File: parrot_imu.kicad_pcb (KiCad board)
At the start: 2 copper layers, 50.8 x 61 mm, 25 parts, among them J1 Conn_01x02_Male, J2 SI-60062-F, J3 TB005-762-02BE, U1 TR05S3V3, U2 VR10S05, U3 Spark_fun_ICM-20948, U4 Teensy4.1, U5 TJA1441AT/0Z, U6 ESDCAN24-2BLY

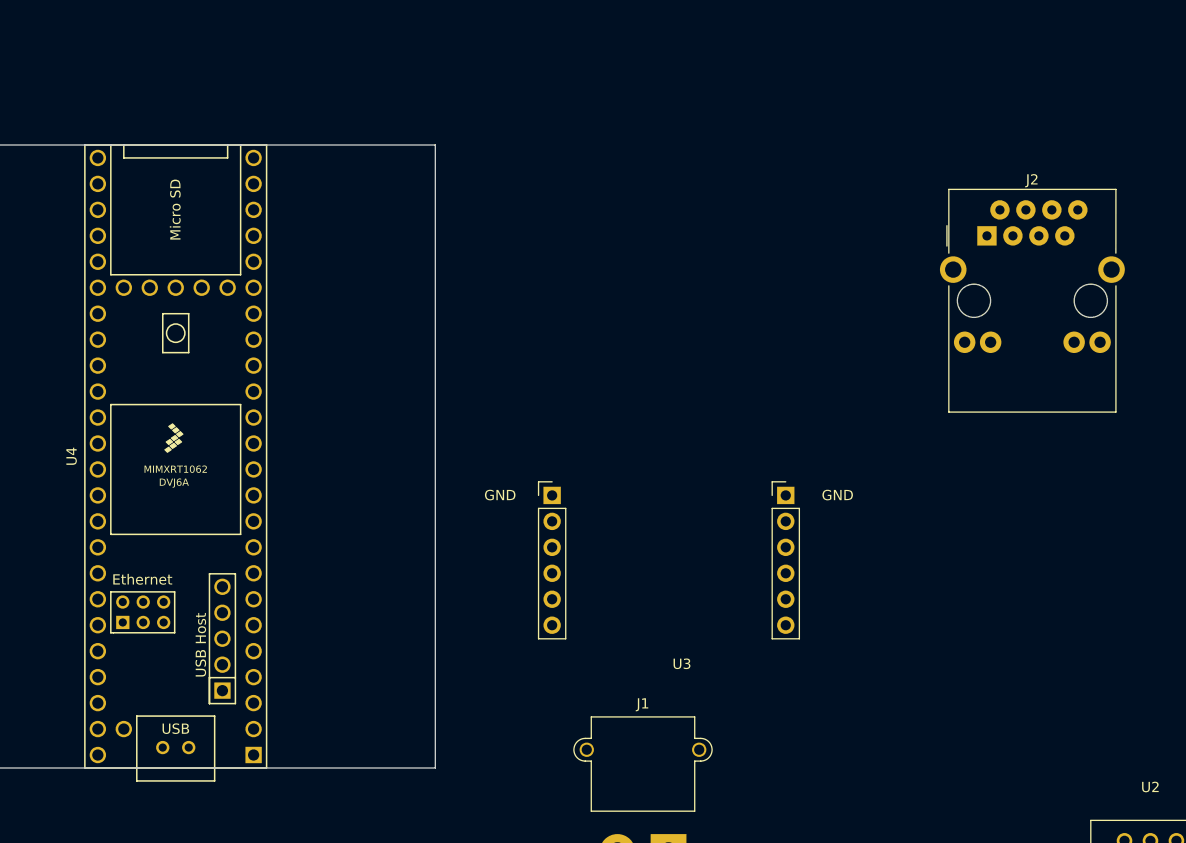
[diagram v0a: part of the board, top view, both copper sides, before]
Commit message: sort out errors with footprints and add mounting holes
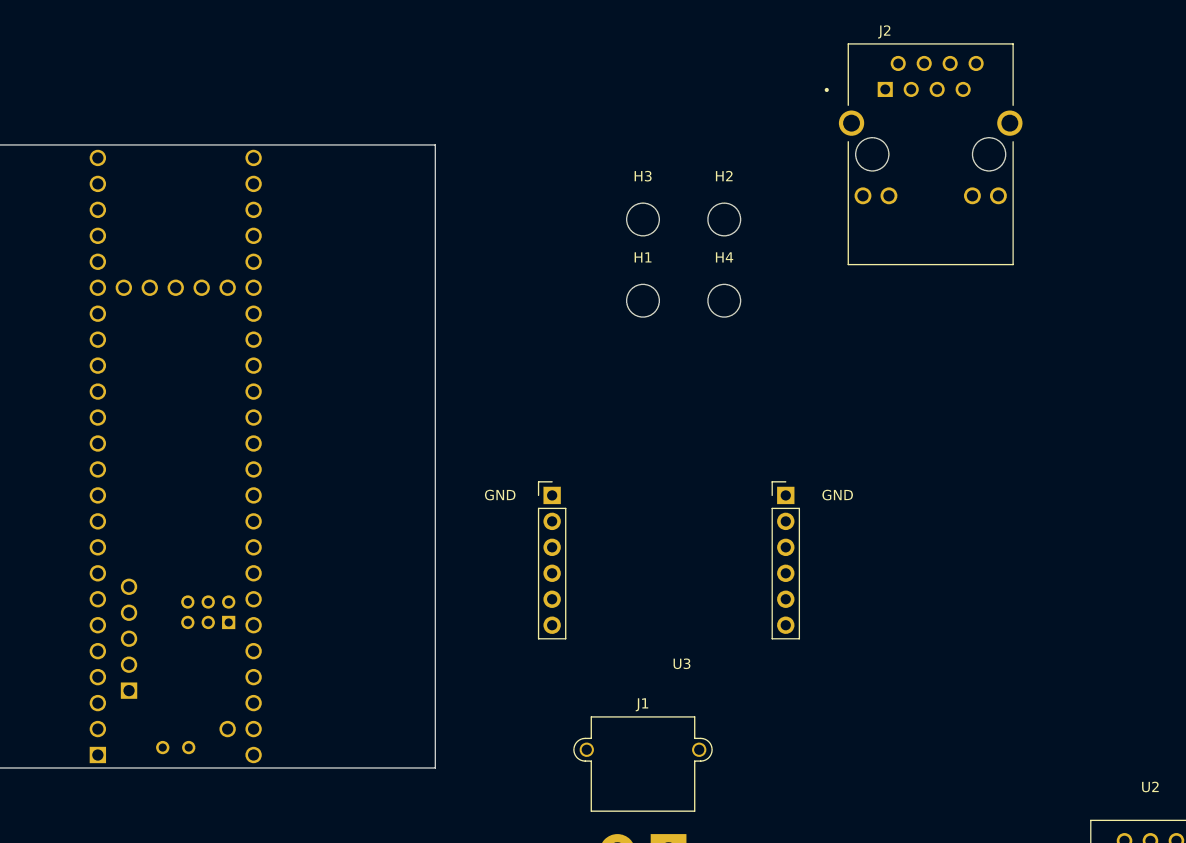
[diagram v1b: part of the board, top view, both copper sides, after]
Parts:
- added H1: MountingHole, MountingHole:MountingHole_3.2mm_M3, F.Cu at (116.8, 63.5)
- added H2: MountingHole, MountingHole:MountingHole_3.2mm_M3, F.Cu at (124.8, 55.5)
- added H3: MountingHole, MountingHole:MountingHole_3.2mm_M3, F.Cu at (116.8, 55.5)
- added H4: MountingHole, MountingHole:MountingHole_3.2mm_M3, F.Cu at (124.8, 63.5)
- J2: footprint Connector_RJ:RJ45_Bel_SI-60062-F -> magjack:BEL_SI-60062-F
- U4: moved to B.Cu
- moved J2 9.69 mm to (145.0, 49.2)

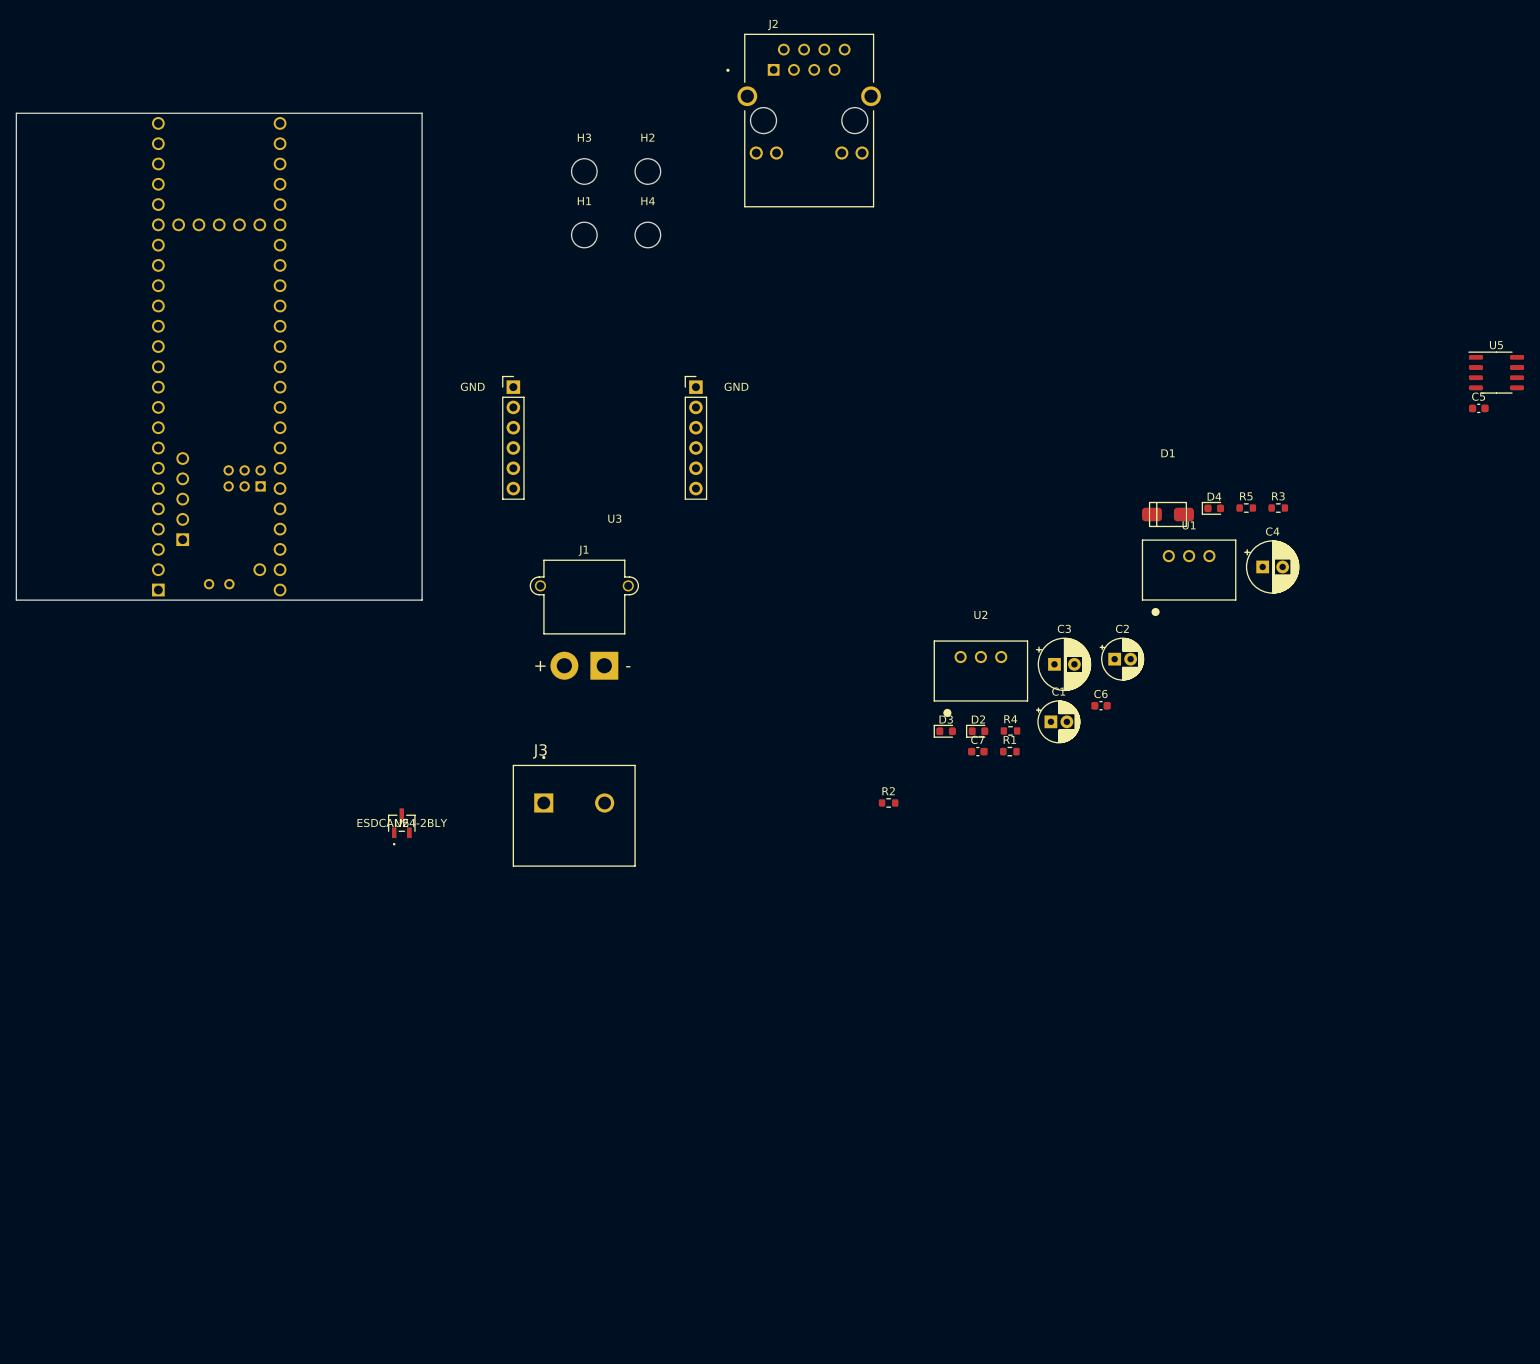
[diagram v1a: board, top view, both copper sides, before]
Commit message: start of laying out components
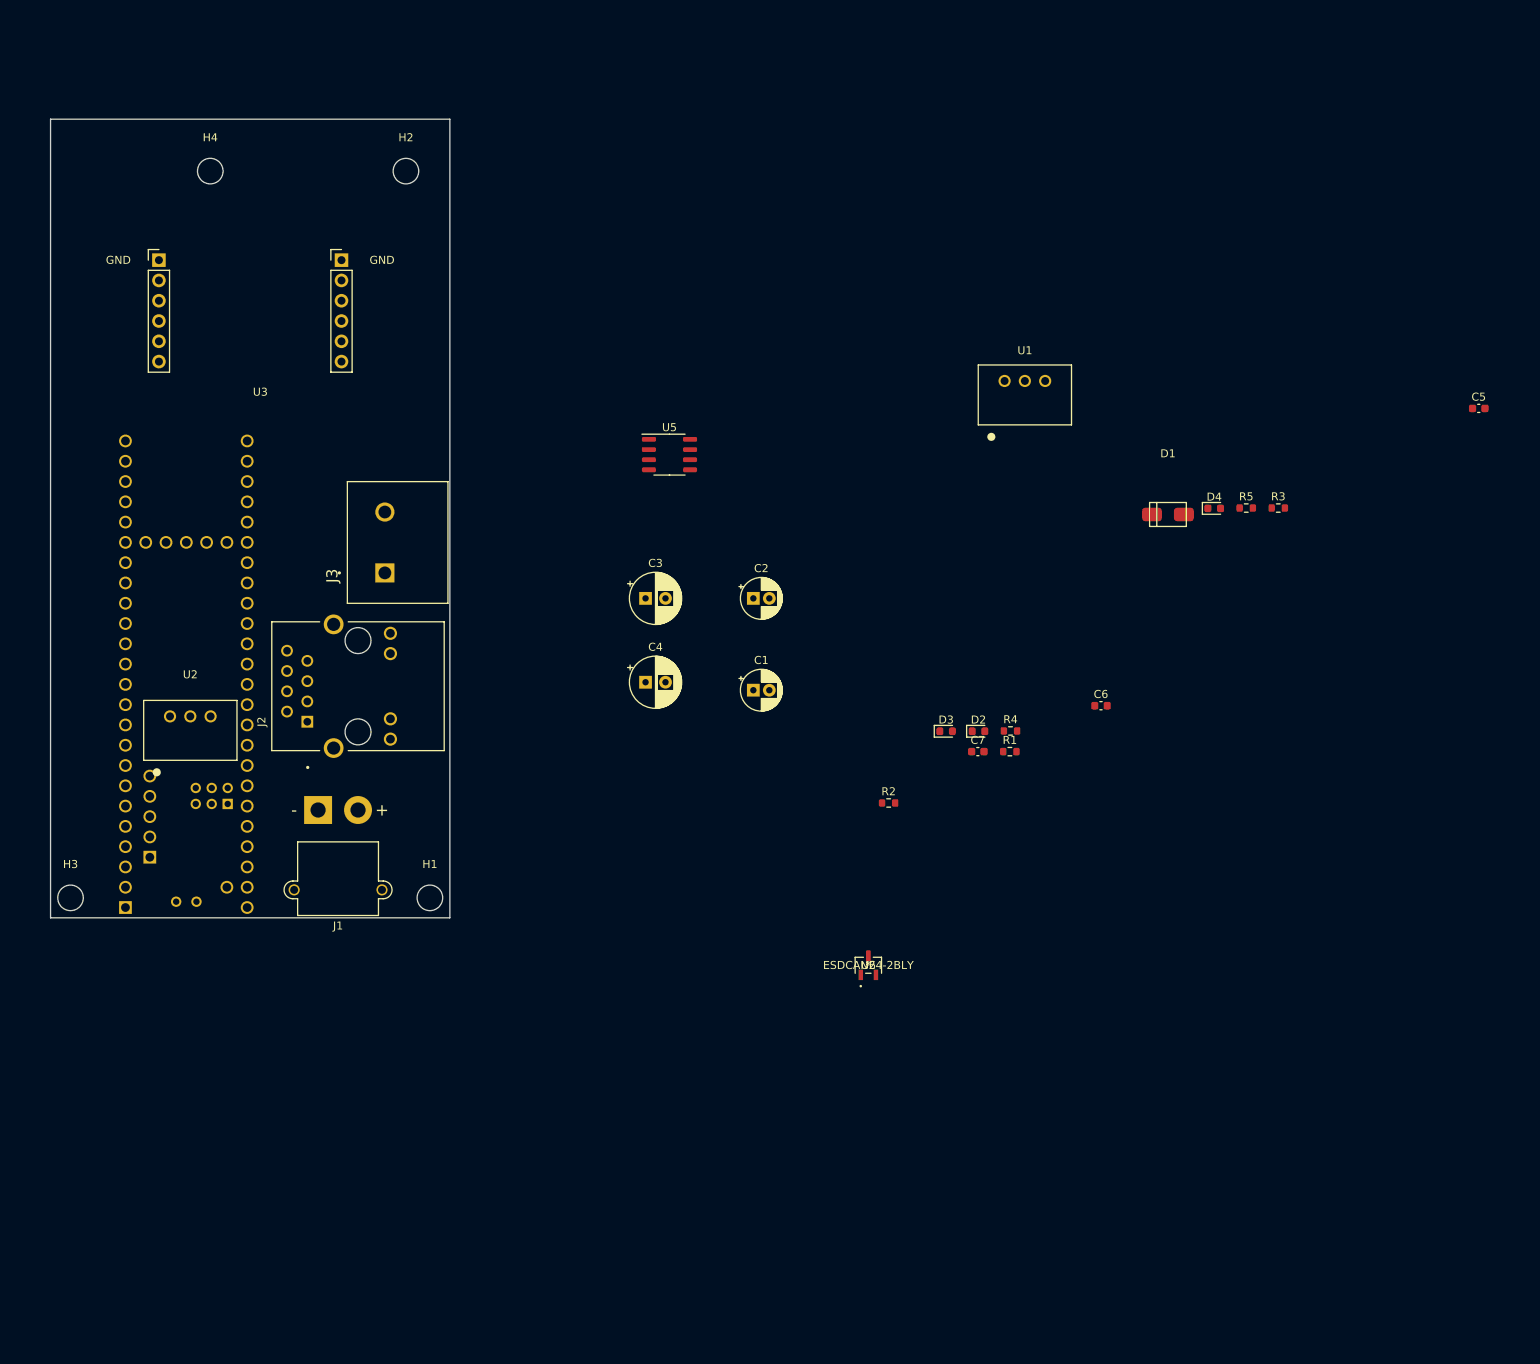
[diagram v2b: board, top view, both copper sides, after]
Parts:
- moved H3 111.4 mm to (52.5, 146.5)
- moved U5 104.1 mm to (127.5, 91.0)
- moved U2 99.3 mm to (67.5, 123.8)
- moved J2 90.6 mm to (88.5, 120.0), turned to 90 degrees
- moved H1 85.2 mm to (97.5, 146.5)
- moved C4 78.6 mm to (124.5, 119.5)
- moved U6 61.1 mm to (152.4, 154.9)
- moved H4 55.4 mm to (70.0, 55.5)
- moved C3 51.9 mm to (124.5, 109.0)
- moved U3 47.1 mm to (86.4, 71.7)
- moved C2 45.9 mm to (138.0, 109.0)
- moved J1 40.1 mm to (83.5, 135.5), turned to 180 degrees
- moved U4 40.0 mm to (67.0, 118.5)
- moved C1 37.5 mm to (138.0, 120.5)
- moved J3 35.0 mm to (91.9, 105.8), turned to 90 degrees
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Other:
- board size 50.8 x 61 mm -> 50 x 100 mm

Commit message: most of pcb and some steps
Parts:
- C6, C7, R4, R5, U5, U6: moved to B.Cu
- J1: footprint Connector_AMASS:AMASS_XT30PW-M_1x02_P2.50mm_Horizontal -> Connector_AMASS:AMASS_XT30PW-F_1x02_P2.50mm_Horizontal
- U4: moved to F.Cu
- moved C5 156.8 mm to (72.0, 82.8), turned to 90 degrees
- moved R3 144.4 mm to (61.5, 122.5), turned to -90 degrees
- moved D4 135.1 mm to (63.2, 124.2), turned to 90 degrees
- moved R5 113.2 mm to (87.3, 84.5), turned to 90 degrees
- moved D1 108.6 mm to (86.0, 130.0)
- moved U1 104.6 mm to (76.5, 124.5), turned to 90 degrees
- moved C7 100.4 mm to (76.5, 82.9), turned to 180 degrees
- moved U6 96.9 mm to (83.7, 86.6), turned to 90 degrees
- moved C6 96.4 mm to (86.5, 106.5), turned to 90 degrees
- moved R4 90.8 mm to (87.3, 88.5), turned to 90 degrees
- moved R1 79.1 mm to (91.0, 126.5), turned to -90 degrees
- moved C2 74.4 mm to (68.5, 135.5), turned to 90 degrees
- moved D3 74.0 mm to (88.5, 118.7), turned to -90 degrees
- moved C3 73.7 mm to (54.0, 130.3), turned to -90 degrees
- moved D2 73.2 mm to (93.0, 126.4), turned to -90 degrees
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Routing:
- net /MOSI: track 0.00 -> 60.4 mm
- net /CS: track 0.00 -> 59.7 mm
- net /SCK: track 0.00 -> 58.9 mm
- net /MISO: track 0.00 -> 57.7 mm
- net /Eth_led: track 0.00 -> 54.3 mm
- net Net-(C1-Pad1): track 0.00 -> 51.2 mm
- net /Eth_tx-: track 0.00 -> 44.6 mm
- net /Eth_tx+: track 0.00 -> 44.0 mm
- net /Eth_rx+: track 0.00 -> 40.7 mm
- net /Eth_rx-: track 0.00 -> 34.7 mm
- net /Can_rx: track 0.00 -> 21.4 mm
- net /Can_tx: track 0.00 -> 21.2 mm
- net +3.3V: track 0.00 -> 17.5 mm, vias 0 -> 1
- net +5V: track 0.00 -> 14.7 mm, vias 0 -> 1
- net GND: track 0.00 -> 8.23 mm, vias 0 -> 4
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- added copper zone on F.Cu, net +3.3V
- added copper zone on F.Cu, net +5V
- added copper zone on B.Cu, net GND

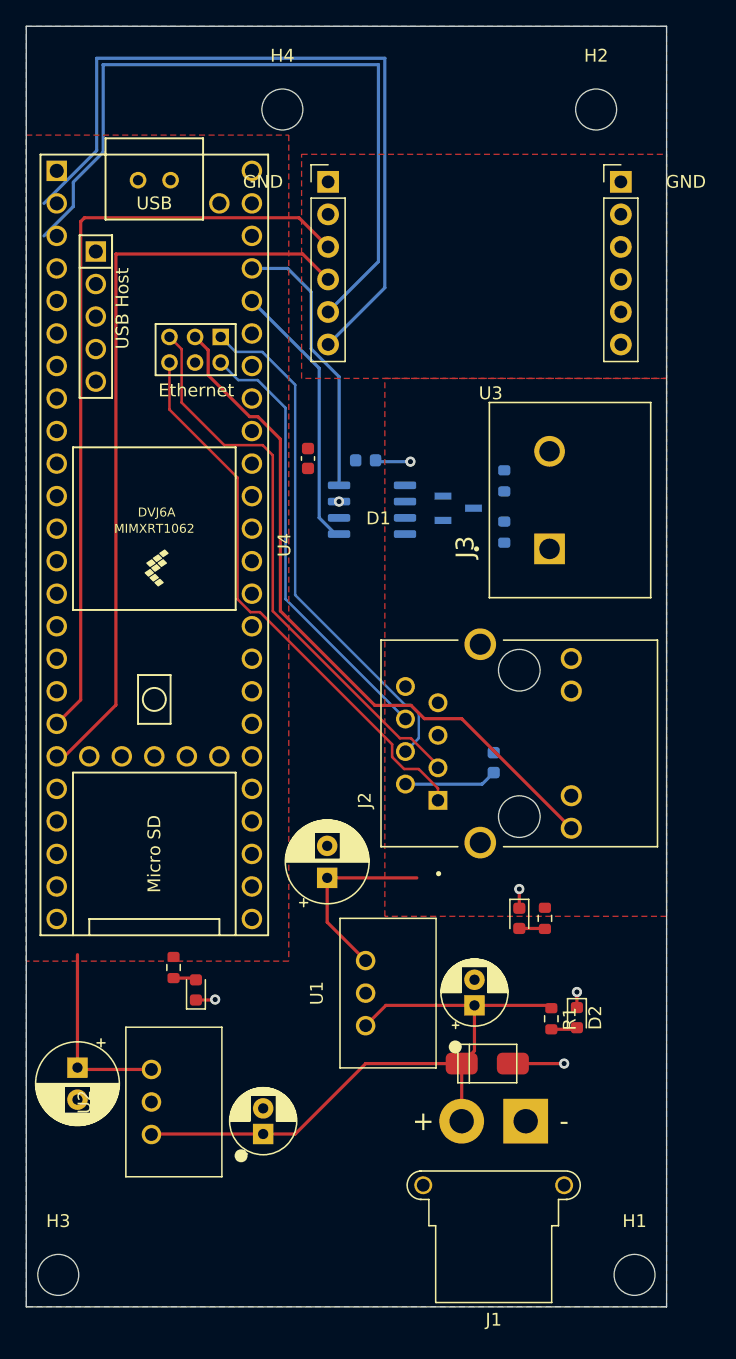
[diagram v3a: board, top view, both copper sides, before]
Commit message: completed draft pcb and added model for imu
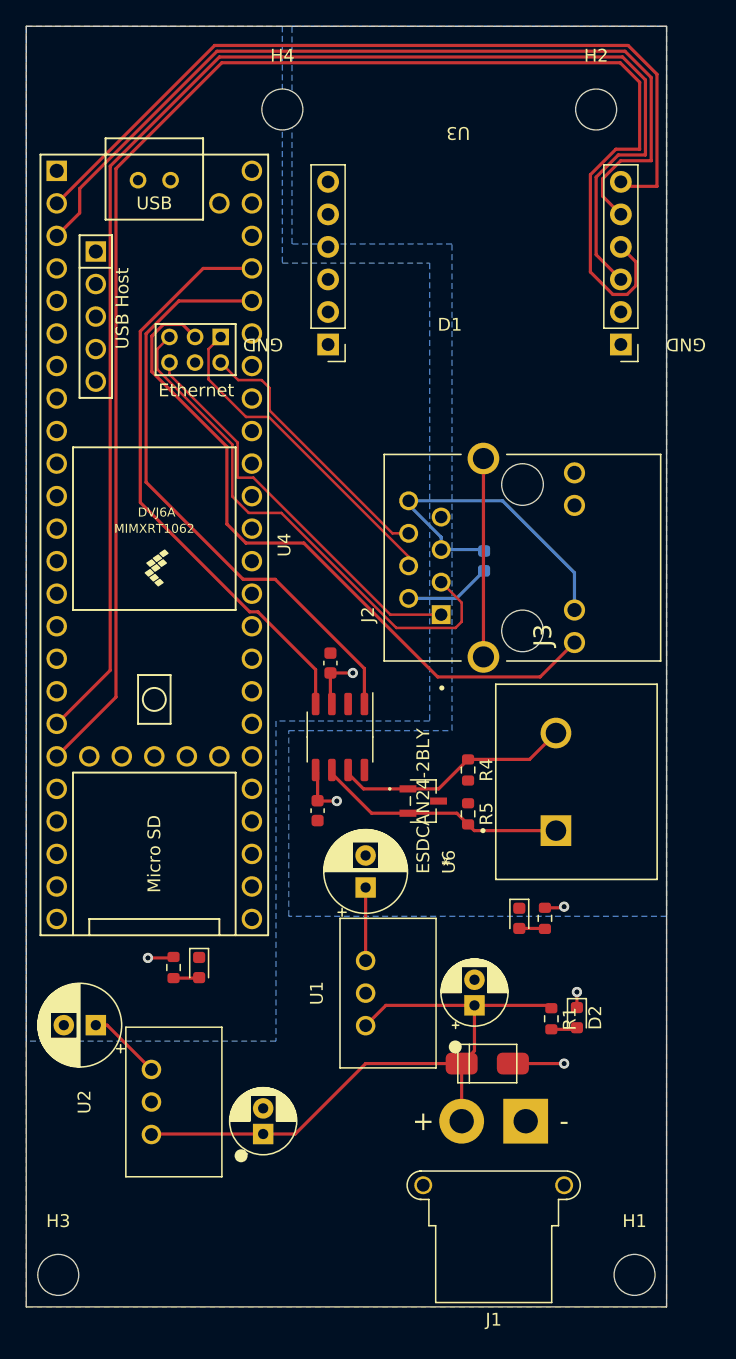
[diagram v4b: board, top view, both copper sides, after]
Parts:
- C7, R4, R5, U5, U6: moved to F.Cu
- moved C7 27.6 mm to (72.8, 110.2), turned to -90 degrees
- moved R5 26.2 mm to (84.5, 110.5), turned to -90 degrees
- moved U6 23.0 mm to (81.0, 109.5), turned to -90 degrees
- moved U3 23.0 mm to (73.6, 68.8), turned to 180 degrees
- moved J3 22.0 mm to (91.4, 111.8)
- moved R4 18.8 mm to (84.5, 107.1), turned to -90 degrees
- moved U5 17.9 mm to (74.5, 104.5), turned to -90 degrees
- moved C5 16.1 mm to (73.8, 98.7)
- moved C6 15.8 mm to (85.8, 90.8)
- moved J2 14.5 mm to (88.8, 90.5)
- moved C3 3.61 mm to (55.4, 127.0), turned to 180 degrees
- moved C4 3.09 mm to (76.5, 116.2)
- moved D4 1.77 mm to (63.5, 122.5), turned to -90 degrees
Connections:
- J3 pad 2: Net-(J3-Pad2) -> Net-(R4-Pad1)
- R4 pad 1: Net-(J3-Pad1) -> Net-(R4-Pad1)
- R5 pad 2: Net-(J3-Pad2) -> Net-(J3-Pad1)
- U5 pad 6: Net-(J3-Pad2) -> Net-(J3-Pad1)
- U5 pad 7: Net-(J3-Pad1) -> Net-(R4-Pad1)
- U6 pad 1: Net-(J3-Pad1) -> Net-(R4-Pad1)
- U6 pad 2: Net-(J3-Pad2) -> Net-(J3-Pad1)
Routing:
- net /SCK: track 58.9 -> 118.3 mm
- net /MOSI: track 60.4 -> 110.6 mm
- net /Can_tx: track 21.2 -> 46.8 mm
- net /Can_rx: track 21.4 -> 45.9 mm
- net GND: track 8.23 -> 31.7 mm, vias 4 -> 2
- net Net-(J3-Pad1): track 0.00 -> 19.6 mm
- net Net-(R4-Pad1): track 0.00 -> 18.8 mm
- net unconnected-(J2-PadS1): track 0.00 -> 15.5 mm
- net /Eth_rx+: track 40.7 -> 25.8 mm
- net /Eth_rx-: track 34.7 -> 21.2 mm
- net /Eth_tx+: track 44.0 -> 31.5 mm
- net /MISO: track 57.7 -> 68.6 mm
- net +3.3V: track 17.5 -> 11.2 mm, vias 1 -> 2
- net /CS: track 59.7 -> 64.6 mm
- net /Eth_tx-: track 44.6 -> 41.4 mm
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- added copper zone on B.Cu, net +3.3V
- added copper zone on B.Cu, net +5V
- added copper zone on F.Cu, net GND
- removed copper zone on F.Cu, net +3.3V
- removed copper zone on F.Cu, net +5V
- removed copper zone on B.Cu, net GND
